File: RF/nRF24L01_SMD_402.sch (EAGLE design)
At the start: 21 parts, among them U4 NRF24L01ALT1

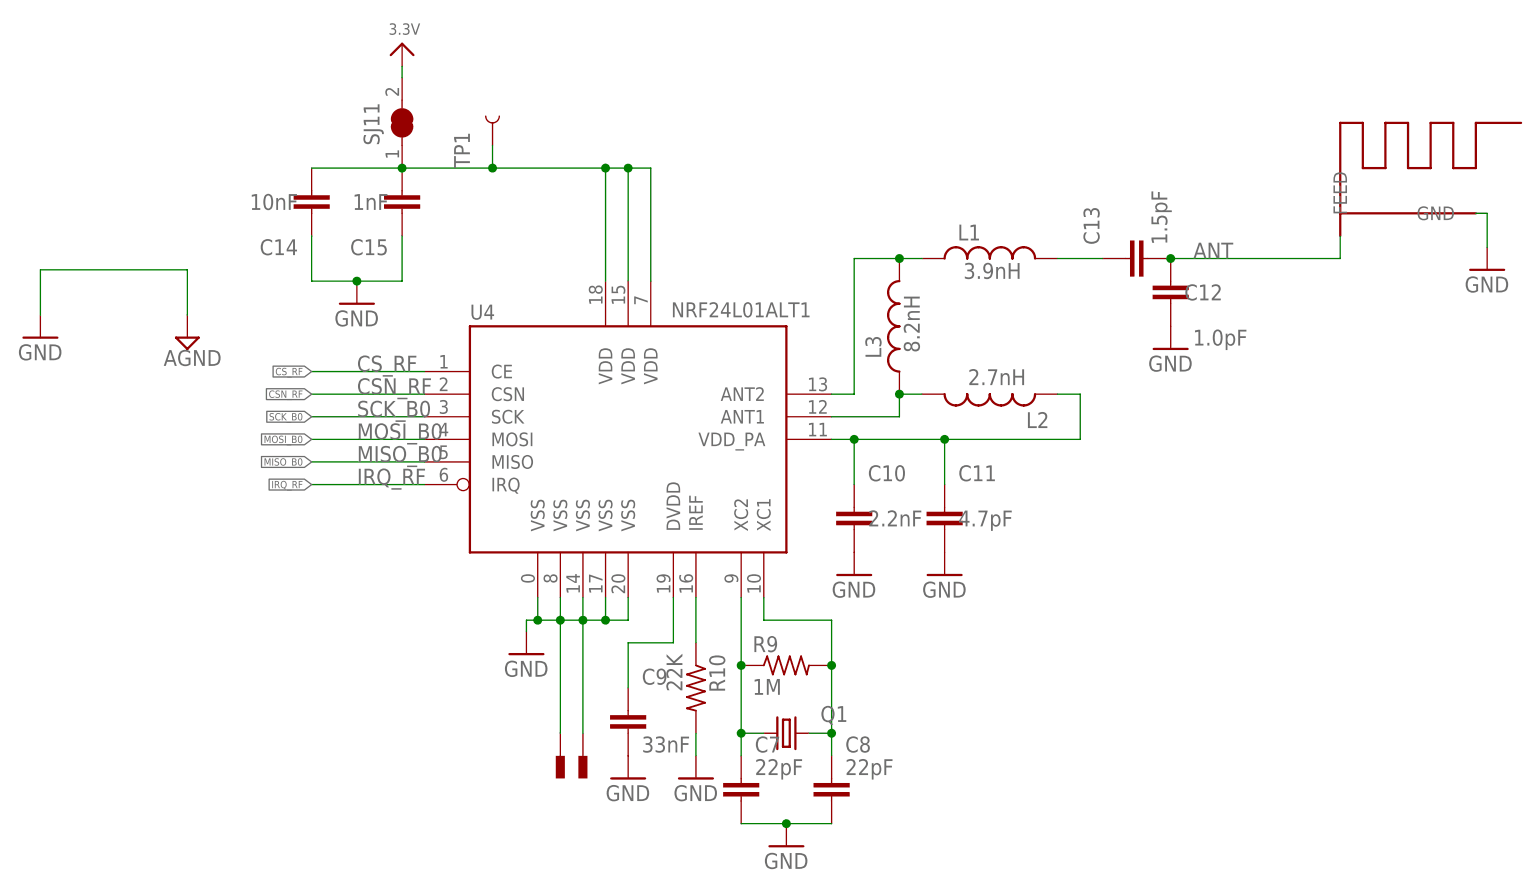
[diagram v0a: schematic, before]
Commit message: nrf ic lib modified
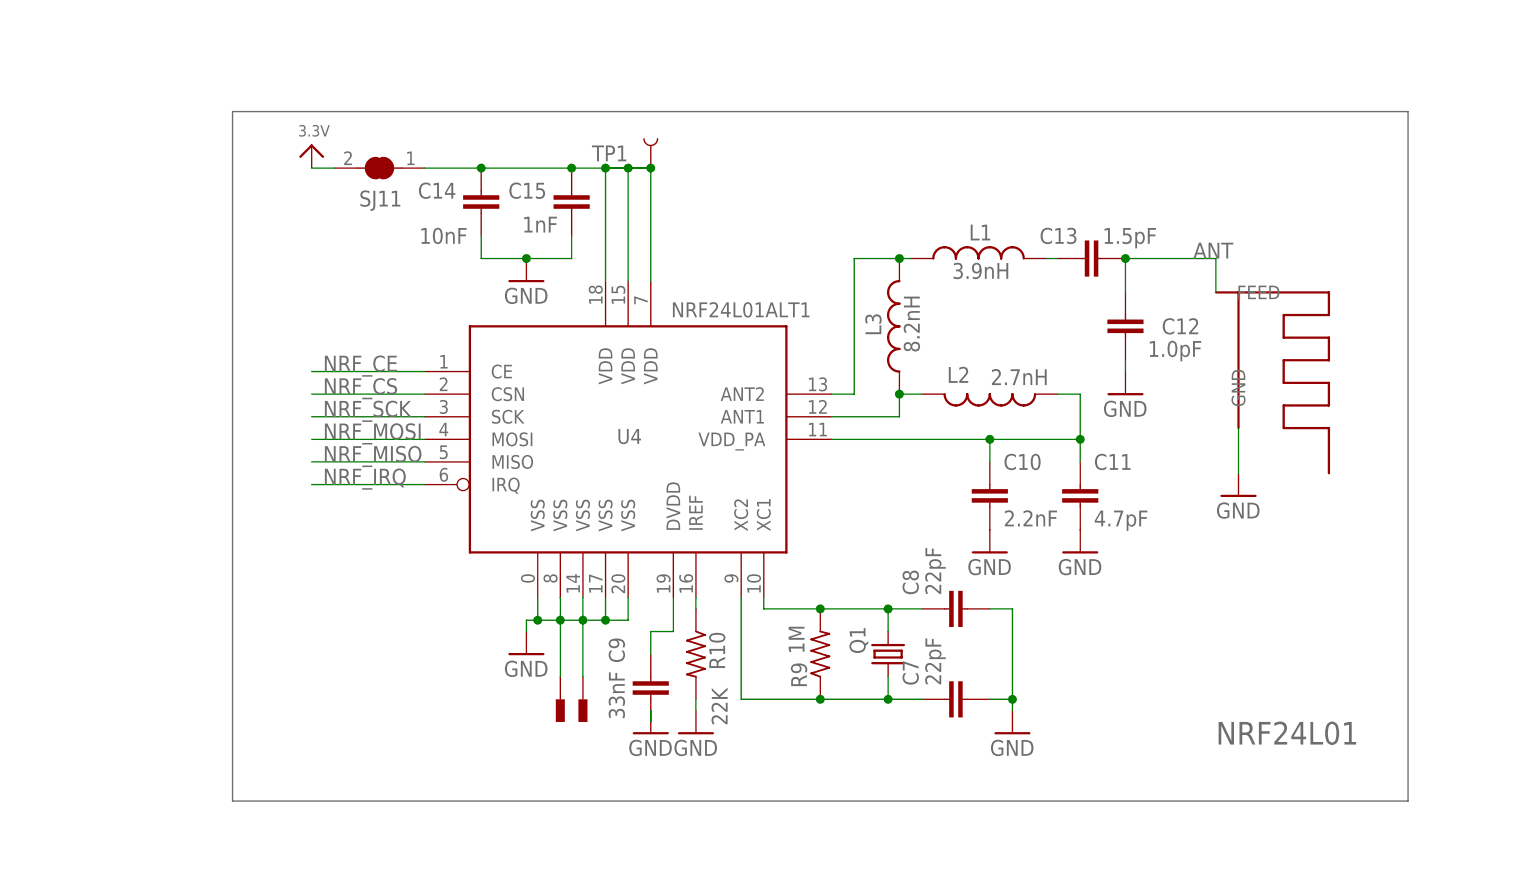
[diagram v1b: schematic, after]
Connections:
- net CSN_RF renamed NRF_CS
- net CS_RF renamed NRF_CE
- net IRQ_RF renamed NRF_IRQ
- net MISO_B0 renamed NRF_MISO
- net MOSI_B0 renamed NRF_MOSI
- net SCK_B0 renamed NRF_SCK
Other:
- note added: "NRF24L01"
- moved on the sheet: C10, C11, C12, C13, C14, C15, C7, C8, C9, L1, Q1, R10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
